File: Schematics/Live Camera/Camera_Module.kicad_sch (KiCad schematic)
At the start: 93 parts, among them J1 Stack Male Edge Connector, J2 SWD_01x04_Pin, J4 Therm_In, J4 USB_C_Female_USB2_Small, J5 VTX, J6 RunCam6, J7 VTX_BATT_IN, J8 VTX_BATT_SWITCH, Q3 AO3401A, Q4 AO3400A, Q5 AO3401A, Q6 AO3401A, SW1 SW_STM_RESET, SW2 SW_STM_BOOT_MODE, U1 CP2102N-Axx-xQFN28, U1 LM66100DCKR, U1 STM32F103CBT6, U12 AMS1117-3.3, U2 TPM8837C-SO1R, U3 W25Q128JVS, U5 LM66100DCKR, U6 LM66100DCKR, U8 ISO1042BDWVR, Y1 X322516MMB4SI

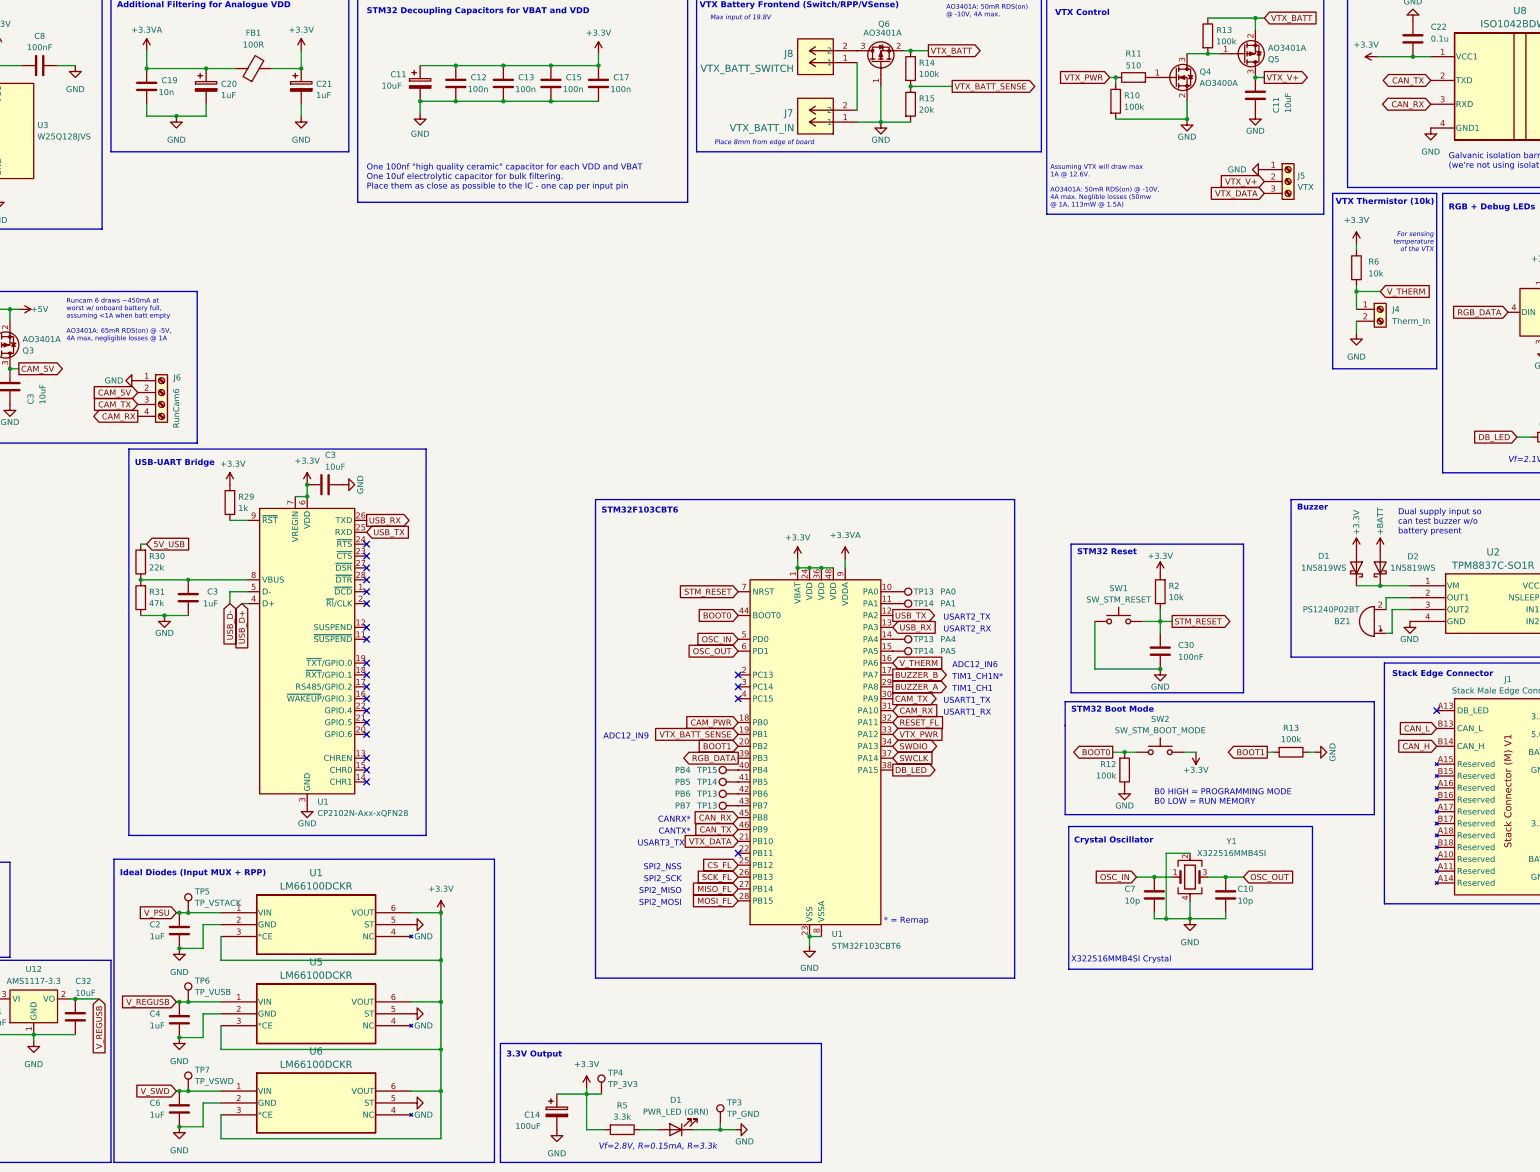
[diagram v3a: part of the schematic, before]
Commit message: Refined & finalized PCB layout
Moved connectors all to the edge of the PCB to make access easier, beefed up several traces, optimized trace paths to minimize traces on the rear ground plane. Removed a few redundant test points too.
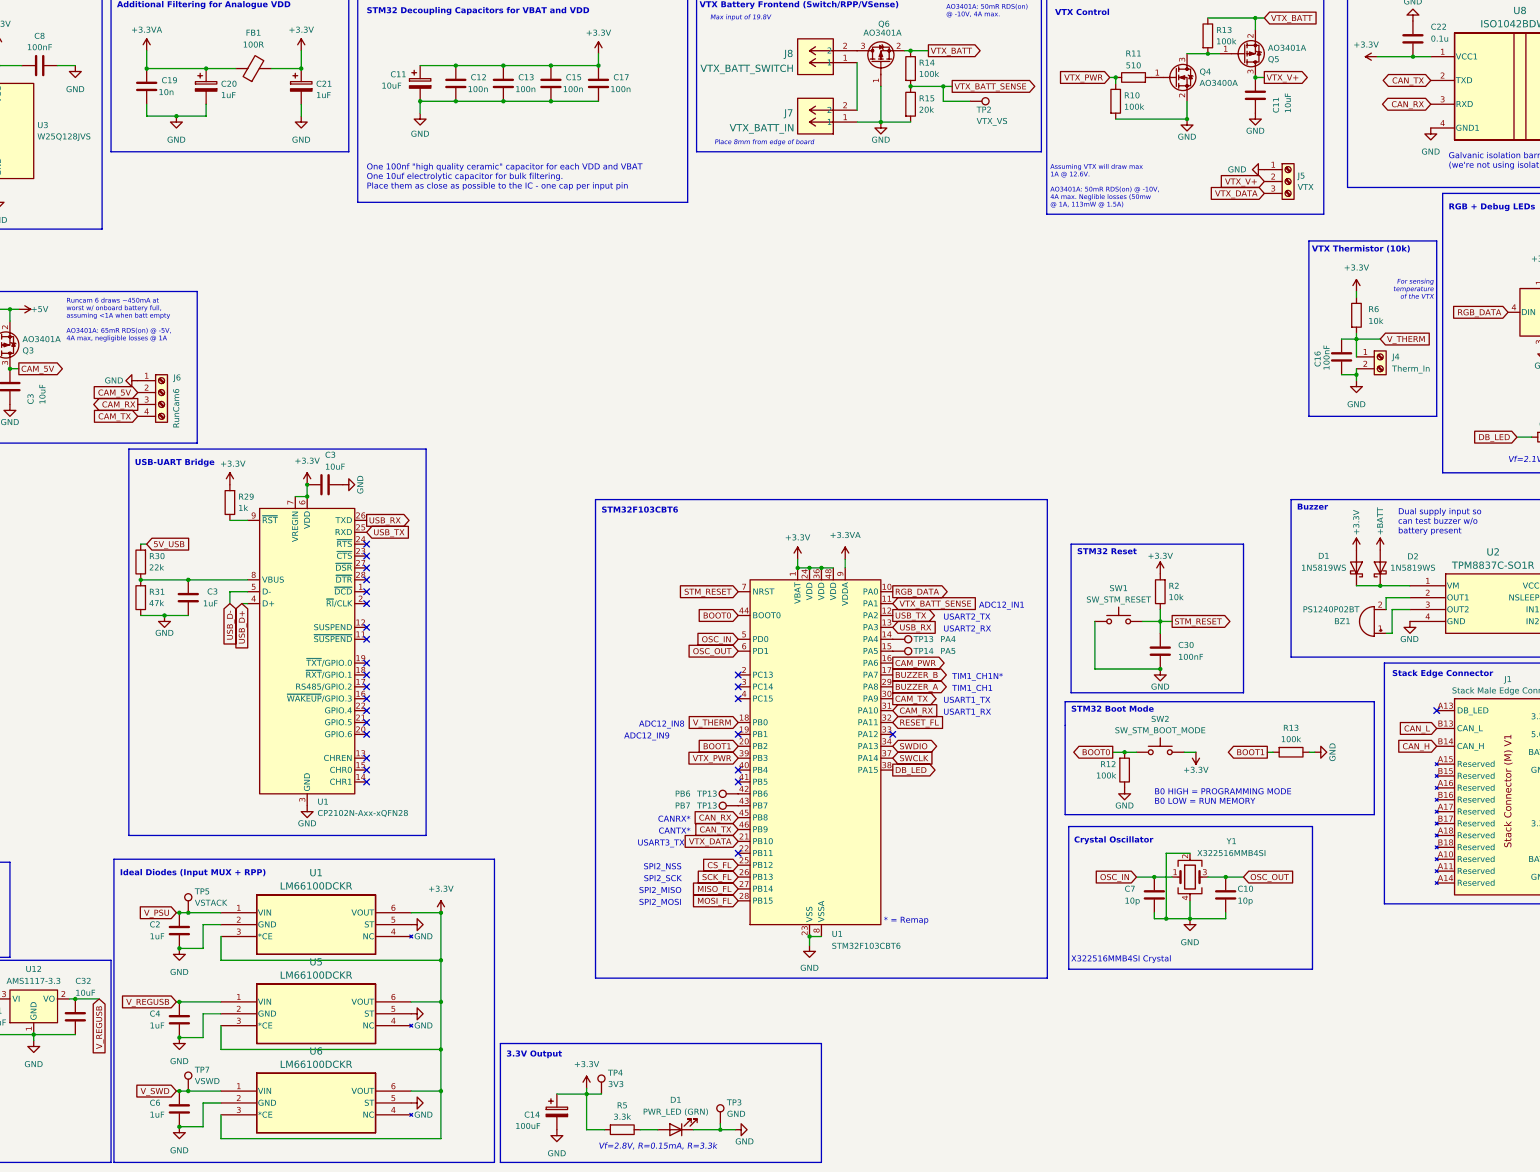
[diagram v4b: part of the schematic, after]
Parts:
- removed TP13: PA0, TestPoint:TestPoint_Pad_1.5x1.5mm, symbol Connector:TestPoint
- removed TP14: PA1, TestPoint:TestPoint_Pad_1.5x1.5mm, symbol Connector:TestPoint
- removed TP14: PB5, TestPoint:TestPoint_Pad_1.5x1.5mm, symbol Connector:TestPoint
- removed TP15: PB4, TestPoint:TestPoint_Pad_1.5x1.5mm, symbol Connector:TestPoint
- removed TP6: TP_VUSB, TestPoint:TestPoint_Pad_1.5x1.5mm, symbol Connector:TestPoint
- added C16: 100nF, Capacitor_SMD:C_0603_1608Metric, symbol Device:C
- added TP2: VTX_VS, TestPoint:TestPoint_Pad_1.0x1.0mm, symbol Connector:TestPoint
- TP3: value TP_GND -> GND
- TP4: value TP_3V3 -> 3V3
- TP5: value TP_VSTACK -> VSTACK
- TP7: value TP_VSWD -> VSWD
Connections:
- net CAM_PWR: now also U1.16 (PA6); no longer U1.18 (PB0)
- net CAM_RX: now also J6.3 (Pin_3); no longer J6.4 (Pin_4)
- net CAM_TX: now also J6.4 (Pin_4); no longer J6.3 (Pin_3)
- net GND: now also C16.1
- net RGB_DATA: now also U1.10 (PA0); no longer U1.39 (PB3)
- net VTX_BATT_SENSE: now also U1.11 (PA1), TP2.1; no longer U1.19 (PB1)
- net VTX_PWR: now also U1.39 (PB3); no longer U1.33 (PA12)
- net V_THERM: now also U1.18 (PB0), C16.2; no longer U1.16 (PA6)
- no-connect marks 30 -> 34
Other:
- note added: "ADC12_IN1"
- note added: "ADC12_IN8"
- note removed: "ADC12_IN6"
- moved on the sheet: J4, R6

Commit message: Quick maintenance
- Changed USB-C port to new one (C5178541)
- Moved VTX battery/switch connectors 4mm forward
- Added polarity markers to VTX battery/switch connectors
- Tweaked silkscreen
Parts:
- J4: JLCPCB C2936184 -> C5178541
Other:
- title: QRET 24-25 SRAD Camera Module (FizzBuzz? Ocellus?) -> QRET 24-25 SRAD Camera Module (Ocellus)
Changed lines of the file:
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@@
 	(paper "B")
 	(title_block
-		(title "QRET 24-25 SRAD Camera Module (FizzBuzz? Ocellus?)")
-		(date "2025-02-26")
+		(title "QRET 24-25 SRAD Camera Module (Ocellus)")
+		(date "2025-03-06")
 		(rev "V1.0")
 		(company "Queen's Rocket Engineering Team")
@@
 			)
 		)
-		(property "JLCPCB" "C2936184"
+		(property "JLCPCB" "C5178541"
 			(at 21.59 248.285 0)
 			(effects

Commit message: Final silkscreen update
Also reverted JLCPCB fields back to LCSC fields for JLCPCB export plugin purposes.
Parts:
- C10, C7: JLCPCB C1634 -> (none); LCSC (none) -> C1634
- C11, C3, C31, C32: JLCPCB C96446 -> (none); LCSC (none) -> C96446
- C12, C13, C15, C17: JLCPCB C1525 -> (none); LCSC (none) -> C1525
- C16, C22, C23, C30, C6, C8: JLCPCB C14663 -> (none); LCSC (none) -> C14663
- C19: JLCPCB C57112 -> (none); LCSC (none) -> C57112
- C2, C3, C4, C6: JLCPCB C15849 -> (none); LCSC (none) -> C15849
- C20, C21: JLCPCB C28323 -> (none); LCSC (none) -> C28323
- D1, D2: JLCPCB C191023 -> (none); LCSC (none) -> C191023
- D1: JLCPCB C2297 -> (none); LCSC (none) -> C2297
- D3: JLCPCB C72038 -> (none); LCSC (none) -> C72038
- FB1: JLCPCB C1015 -> (none); LCSC (none) -> C1015
- J4: JLCPCB C5178541 -> (none); LCSC (none) -> C5178541
- Q3, Q5, Q6: JLCPCB C15127 -> (none); LCSC (none) -> C15127
- Q4: JLCPCB C20917 -> (none); LCSC (none) -> C20917
- R10, R12, R13, R14, R38: JLCPCB C25803 -> (none); LCSC (none) -> C25803
- R11, R39: JLCPCB C23193 -> (none); LCSC (none) -> C23193
- R15: JLCPCB C4184 -> (none); LCSC (none) -> C4184
- R2, R4, R6: JLCPCB C25804 -> (none); LCSC (none) -> C25804
- R28, R29: JLCPCB C23186 -> (none); LCSC (none) -> C23186
- R29: JLCPCB C21190 -> (none); LCSC (none) -> C21190
- R30: JLCPCB C31850 -> (none); LCSC (none) -> C31850
- R31: JLCPCB C25819 -> (none); LCSC (none) -> C25819
- R5: JLCPCB C22978 -> (none); LCSC (none) -> C22978
- R7: JLCPCB C23228 -> (none); LCSC (none) -> C23228
- R8: JLCPCB C22843 -> (none); LCSC (none) -> C22843
- SW1, SW2: JLCPCB C318884 -> (none); LCSC (none) -> C318884
- U1, U5, U6: JLCPCB C2869734 -> (none); LCSC (none) -> C2869734
- U1: JLCPCB C6568 -> (none); LCSC (none) -> C6568
- U1: JLCPCB C8304 -> (none); LCSC (none) -> C8304
- U12: JLCPCB C6186 -> (none); LCSC (none) -> C6186
- U3: JLCPCB C97521 -> (none); LCSC (none) -> C97521
- U8: JLCPCB C484409 -> (none); LCSC (none) -> C484409
- Y1: JLCPCB C13738 -> (none); LCSC (none) -> C13738
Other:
- title: QRET 24-25 SRAD Camera Module (Ocellus) -> QRET 24-25 SRAD Camera Module
